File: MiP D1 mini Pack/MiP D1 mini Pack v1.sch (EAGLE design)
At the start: 6 parts, among them J2 D1 mini, J3 Debug

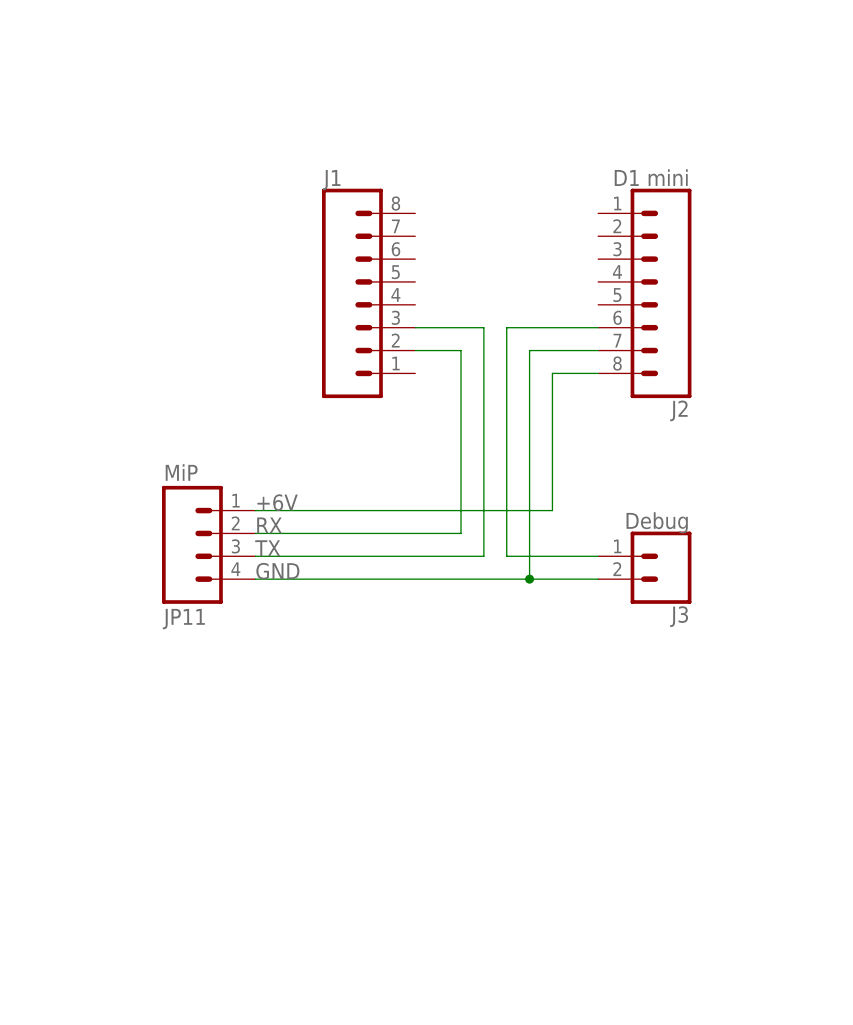
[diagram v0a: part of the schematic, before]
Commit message: Moved the debug connector
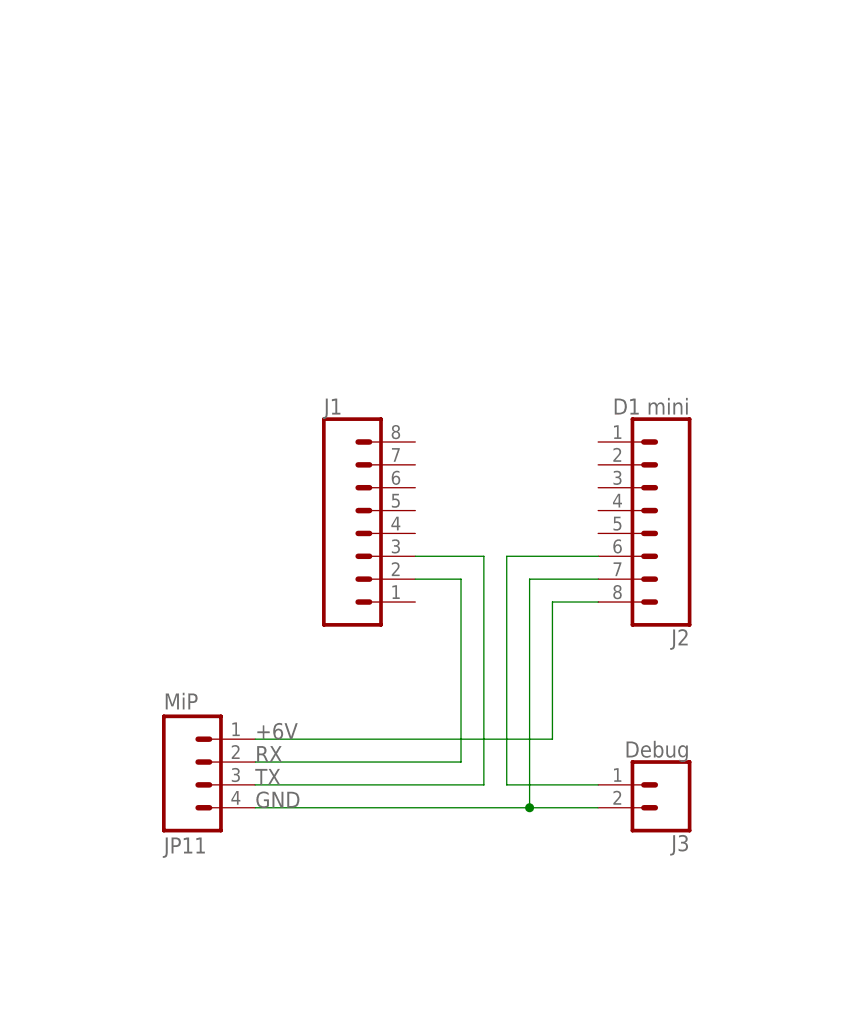
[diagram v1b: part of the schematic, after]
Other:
- moved on the sheet: J1, J2, J3, JP11
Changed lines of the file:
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@@
 <instance part="FRAME1" gate="G$1" x="0" y="0"/>
 <instance part="FRAME1" gate="G$2" x="147.32" y="0"/>
-<instance part="JP11" gate="G$1" x="96.52" y="114.3" rot="MR180"/>
+<instance part="JP11" gate="G$1" x="96.52" y="88.9" rot="MR180"/>
 <instance part="LOGO2" gate="G$1" x="233.68" y="48.26"/>
-<instance part="J1" gate="G$1" x="114.3" y="139.7"/>
-<instance part="J2" gate="G$1" x="144.78" y="142.24" rot="R180"/>
-<instance part="J3" gate="G$1" x="147.32" y="111.76" rot="R180"/>
+<instance part="J1" gate="G$1" x="114.3" y="114.3"/>
+<instance part="J2" gate="G$1" x="144.78" y="116.84" rot="R180"/>
+<instance part="J3" gate="G$1" x="147.32" y="86.36" rot="R180"/>
 </instances>
 <busses>
@@
 <segment>
 <pinref part="J3" gate="G$1" pin="1"/>
-<wire x1="139.7" y1="111.76" x2="129.54" y2="111.76" width="0.1524" layer="91"/>
-<wire x1="129.54" y1="111.76" x2="129.54" y2="137.16" width="0.1524" layer="91"/>
+<wire x1="139.7" y1="86.36" x2="129.54" y2="86.36" width="0.1524" layer="91"/>
+<wire x1="129.54" y1="86.36" x2="129.54" y2="111.76" width="0.1524" layer="91"/>
 <pinref part="J2" gate="G$1" pin="6"/>
-<wire x1="129.54" y1="137.16" x2="139.7" y2="137.16" width="0.1524" layer="91"/>
+<wire x1="129.54" y1="111.76" x2="139.7" y2="111.76" width="0.1524" layer="91"/>
 </segment>
 </net>
@@
 <pinref part="JP11" gate="G$1" pin="4"/>
 <pinref part="J3" gate="G$1" pin="2"/>
-<wire x1="101.6" y1="109.22" x2="132.08" y2="109.22" width="0.1524" layer="91"/>
+<wire x1="101.6" y1="83.82" x2="132.08" y2="83.82" width="0.1524" layer="91"/>
 <pinref part="J2" gate="G$1" pin="7"/>
-<wire x1="132.08" y1="109.22" x2="139.7" y2="109.22" width="0.1524" layer="91"/>
-<wire x1="139.7" y1="134.62" x2="132.08" y2="134.62" width="0.1524" layer="91"/>
-<wire x1="132.08" y1="134.62" x2="132.08" y2="109.22" width="0.1524" layer="91"/>
-<junction x="132.08" y="109.22"/>
-<label x="101.6" y="109.22" size="1.778" layer="95"/>
+<wire x1="132.08" y1="83.82" x2="139.7" y2="83.82" width="0.1524" layer="91"/>
+<wire x1="139.7" y1="109.22" x2="132.08" y2="109.22" width="0.1524" layer="91"/>
+<wire x1="132.08" y1="109.22" x2="132.08" y2="83.82" width="0.1524" layer="91"/>
+<junction x="132.08" y="83.82"/>
+<label x="101.6" y="83.82" size="1.778" layer="95"/>
 </segment>
 </net>
@@
 <segment>
 <pinref part="JP11" gate="G$1" pin="1"/>
-<wire x1="101.6" y1="116.84" x2="134.62" y2="116.84" width="0.1524" layer="91"/>
-<wire x1="134.62" y1="116.84" x2="134.62" y2="132.08" width="0.1524" layer="91"/>
+<wire x1="101.6" y1="91.44" x2="134.62" y2="91.44" width="0.1524" layer="91"/>
+<wire x1="134.62" y1="91.44" x2="134.62" y2="106.68" width="0.1524" layer="91"/>
 <pinref part="J2" gate="G$1" pin="8"/>
-<wire x1="134.62" y1="132.08" x2="139.7" y2="132.08" width="0.1524" layer="91"/>
-<label x="101.6" y="116.84" size="1.778" layer="95"/>
+<wire x1="134.62" y1="106.68" x2="139.7" y2="106.68" width="0.1524" layer="91"/>
+<label x="101.6" y="91.44" size="1.778" layer="95"/>
 </segment>
 </net>
@@
 <segment>
 <pinref part="JP11" gate="G$1" pin="3"/>
-<wire x1="101.6" y1="111.76" x2="127" y2="111.76" width="0.1524" layer="91"/>
-<wire x1="127" y1="111.76" x2="127" y2="137.16" width="0.1524" layer="91"/>
+<wire x1="101.6" y1="86.36" x2="127" y2="86.36" width="0.1524" layer="91"/>
+<wire x1="127" y1="86.36" x2="127" y2="111.76" width="0.1524" layer="91"/>
 <pinref part="J1" gate="G$1" pin="3"/>
-<wire x1="127" y1="137.16" x2="119.38" y2="137.16" width="0.1524" layer="91"/>
-<label x="101.6" y="111.76" size="1.778" layer="95"/>
+<wire x1="127" y1="111.76" x2="119.38" y2="111.76" width="0.1524" layer="91"/>
+<label x="101.6" y="86.36" size="1.778" layer="95"/>
 </segment>
 </net>
@@
 <segment>
 <pinref part="JP11" gate="G$1" pin="2"/>
-<wire x1="101.6" y1="114.3" x2="124.46" y2="114.3" width="0.1524" layer="91"/>
-<wire x1="124.46" y1="114.3" x2="124.46" y2="134.62" width="0.1524" layer="91"/>
+<wire x1="101.6" y1="88.9" x2="124.46" y2="88.9" width="0.1524" layer="91"/>
+<wire x1="124.46" y1="88.9" x2="124.46" y2="109.22" width="0.1524" layer="91"/>
 <pinref part="J1" gate="G$1" pin="2"/>
-<wire x1="124.46" y1="134.62" x2="119.38" y2="134.62" width="0.1524" layer="91"/>
-<label x="101.6" y="114.3" size="1.778" layer="95"/>
+<wire x1="124.46" y1="109.22" x2="119.38" y2="109.22" width="0.1524" layer="91"/>
+<label x="101.6" y="88.9" size="1.778" layer="95"/>
 </segment>
 </net>
